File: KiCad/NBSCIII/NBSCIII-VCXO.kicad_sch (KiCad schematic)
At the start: 20 parts, among them Q1000 BC337-25, Q1001 2SC1906, X1000 6.000Mhz HC49/U

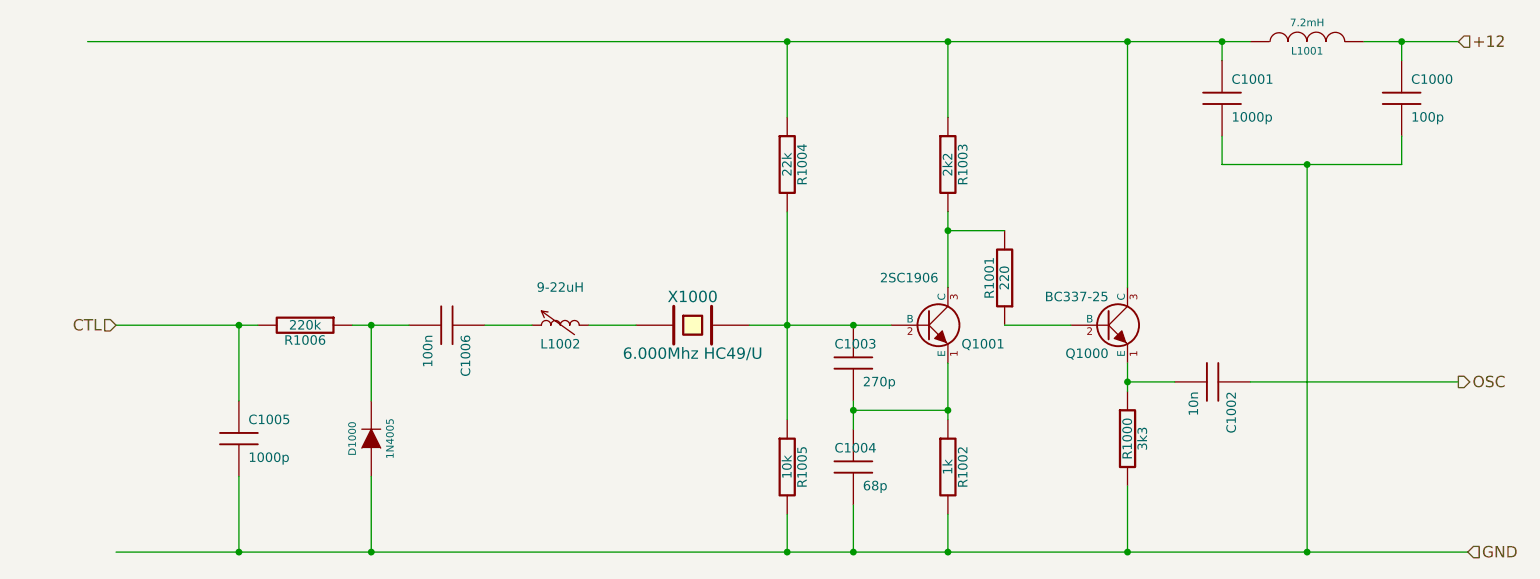
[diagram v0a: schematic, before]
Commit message: unrescue to Device:C
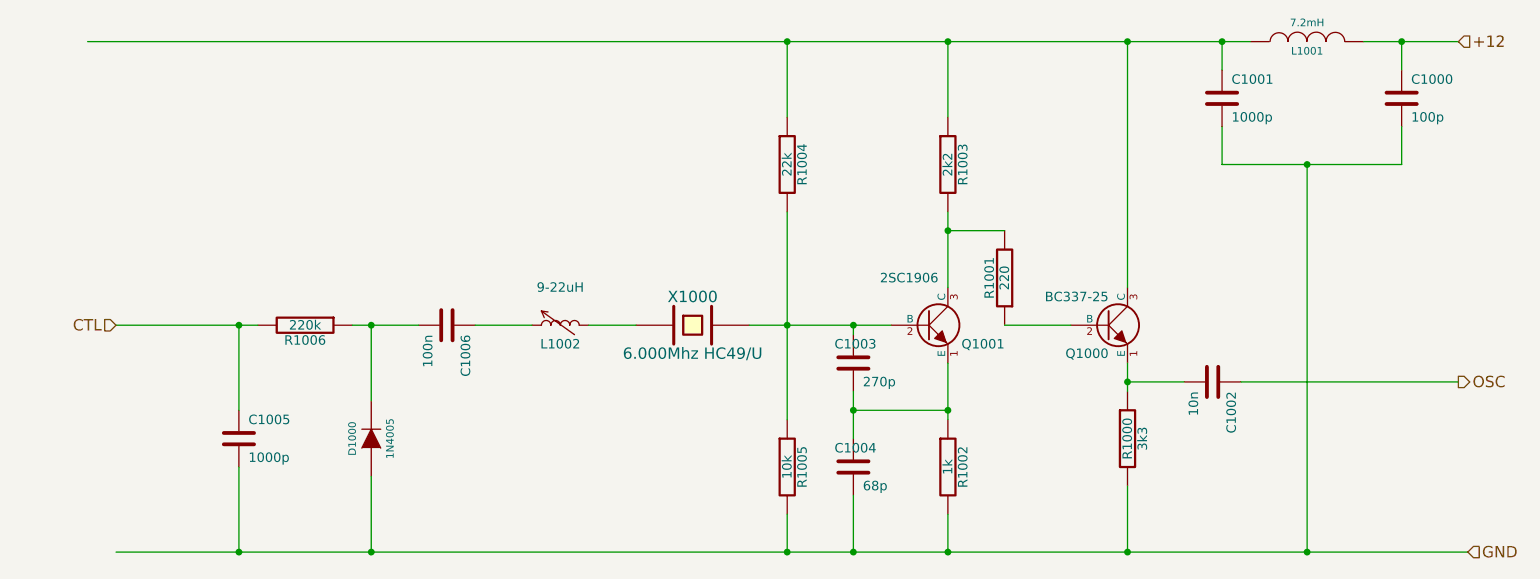
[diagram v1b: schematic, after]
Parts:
- C1000, C1001, C1002, C1003, C1004, C1005, C1006: symbol NBSCIII-rescue:C -> Device:C
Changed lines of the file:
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@@
   (junction (at 219.71 54.61) (diameter 0) (color 0 0 0 0)
   )
+  (junction (at 146.05 92.71) (diameter 0) (color 0 0 0 0)
+  )
   (junction (at 182.88 123.19) (diameter 0) (color 0 0 0 0)
   )
@@
   (junction (at 182.88 100.33) (diameter 0) (color 0 0 0 0)
   )
-  (junction (at 146.05 92.71) (diameter 0) (color 0 0 0 0)
-  )
   (junction (at 207.01 71.12) (diameter 0) (color 0 0 0 0)
   )
@@
   (junction (at 158.75 54.61) (diameter 0) (color 0 0 0 0)
   )
-  (wire (pts (xy 189.23 100.33) (xy 182.88 100.33))
-    (stroke (width 0) (type default) (color 0 0 0 0))
-  )
-  (wire (pts (xy 151.13 92.71) (xy 146.05 92.71))
-    (stroke (width 0) (type default) (color 0 0 0 0))
-  )
-  (wire (pts (xy 195.58 54.61) (xy 195.58 57.15))
+  (wire (pts (xy 146.05 104.14) (xy 146.05 107.95))
+    (stroke (width 0) (type default) (color 0 0 0 0))
+  )
+  (wire (pts (xy 182.88 100.33) (xy 190.5 100.33))
+    (stroke (width 0) (type default) (color 0 0 0 0))
+  )
+  (wire (pts (xy 195.58 54.61) (xy 195.58 58.42))
     (stroke (width 0) (type default) (color 0 0 0 0))
   )
@@
     (stroke (width 0) (type default) (color 0 0 0 0))
   )
-  (wire (pts (xy 86.36 92.71) (xy 81.28 92.71))
+  (wire (pts (xy 81.28 92.71) (xy 87.63 92.71))
     (stroke (width 0) (type default) (color 0 0 0 0))
   )
@@
     (stroke (width 0) (type default) (color 0 0 0 0))
   )
-  (wire (pts (xy 195.58 71.12) (xy 195.58 67.31))
+  (wire (pts (xy 146.05 92.71) (xy 151.13 92.71))
     (stroke (width 0) (type default) (color 0 0 0 0))
   )
@@
     (stroke (width 0) (type default) (color 0 0 0 0))
   )
-  (wire (pts (xy 146.05 106.68) (xy 146.05 104.14))
-    (stroke (width 0) (type default) (color 0 0 0 0))
-  )
   (wire (pts (xy 195.58 54.61) (xy 182.88 54.61))
     (stroke (width 0) (type default) (color 0 0 0 0))
@@
     (stroke (width 0) (type default) (color 0 0 0 0))
   )
+  (wire (pts (xy 219.71 54.61) (xy 219.71 58.42))
+    (stroke (width 0) (type default) (color 0 0 0 0))
+  )
   (wire (pts (xy 182.88 101.6) (xy 182.88 100.33))
     (stroke (width 0) (type default) (color 0 0 0 0))
   )
-  (wire (pts (xy 146.05 104.14) (xy 146.05 102.87))
+  (wire (pts (xy 146.05 101.6) (xy 146.05 104.14))
     (stroke (width 0) (type default) (color 0 0 0 0))
   )
@@
     (stroke (width 0) (type default) (color 0 0 0 0))
   )
-  (wire (pts (xy 219.71 54.61) (xy 219.71 57.15))
-    (stroke (width 0) (type default) (color 0 0 0 0))
-  )
   (wire (pts (xy 207.01 123.19) (xy 228.6 123.19))
     (stroke (width 0) (type default) (color 0 0 0 0))
   )
-  (wire (pts (xy 96.52 92.71) (xy 102.87 92.71))
+  (wire (pts (xy 95.25 92.71) (xy 102.87 92.71))
     (stroke (width 0) (type default) (color 0 0 0 0))
   )
@@
     (stroke (width 0) (type default) (color 0 0 0 0))
   )
-  (wire (pts (xy 219.71 67.31) (xy 219.71 71.12))
+  (wire (pts (xy 219.71 66.04) (xy 219.71 71.12))
     (stroke (width 0) (type default) (color 0 0 0 0))
   )
@@
     (stroke (width 0) (type default) (color 0 0 0 0))
   )
-  (wire (pts (xy 146.05 92.71) (xy 137.16 92.71))
-    (stroke (width 0) (type default) (color 0 0 0 0))
-  )
-  (wire (pts (xy 146.05 123.19) (xy 146.05 116.84))
+  (wire (pts (xy 137.16 92.71) (xy 146.05 92.71))
+    (stroke (width 0) (type default) (color 0 0 0 0))
+  )
+  (wire (pts (xy 195.58 66.04) (xy 195.58 71.12))
+    (stroke (width 0) (type default) (color 0 0 0 0))
+  )
+  (wire (pts (xy 146.05 115.57) (xy 146.05 123.19))
     (stroke (width 0) (type default) (color 0 0 0 0))
   )
@@
     (stroke (width 0) (type default) (color 0 0 0 0))
   )
-  (wire (pts (xy 63.5 113.03) (xy 63.5 123.19))
-    (stroke (width 0) (type default) (color 0 0 0 0))
-  )
   (wire (pts (xy 137.16 54.61) (xy 43.18 54.61))
     (stroke (width 0) (type default) (color 0 0 0 0))
@@
     (stroke (width 0) (type default) (color 0 0 0 0))
   )
-  (wire (pts (xy 63.5 92.71) (xy 63.5 102.87))
+  (wire (pts (xy 63.5 92.71) (xy 63.5 104.14))
     (stroke (width 0) (type default) (color 0 0 0 0))
   )
@@
     (stroke (width 0) (type default) (color 0 0 0 0))
   )
+  (wire (pts (xy 63.5 111.76) (xy 63.5 123.19))
+    (stroke (width 0) (type default) (color 0 0 0 0))
+  )
+  (wire (pts (xy 146.05 92.71) (xy 146.05 93.98))
+    (stroke (width 0) (type default) (color 0 0 0 0))
+  )
   (wire (pts (xy 219.71 71.12) (xy 207.01 71.12))
     (stroke (width 0) (type default) (color 0 0 0 0))
   )
-  (wire (pts (xy 199.39 100.33) (xy 227.33 100.33))
+  (wire (pts (xy 198.12 100.33) (xy 227.33 100.33))
     (stroke (width 0) (type default) (color 0 0 0 0))
   )
@@
     (pin "2")
   )
-  (symbol (lib_id "NBSCIII-rescue:C") (at 195.58 62.23 0) (unit 1)
+  (symbol (lib_id "Device:C") (at 195.58 62.23 0) (unit 1)
     (in_bom yes) (on_board yes)
     (property "Reference" "C1001" (id 0) (at 196.85 59.69 0)
@@
     (pin "2")
   )
-  (symbol (lib_id "NBSCIII-rescue:C") (at 219.71 62.23 0) (unit 1)
+  (symbol (lib_id "Device:C") (at 219.71 62.23 0) (unit 1)
     (in_bom yes) (on_board yes)
     (property "Reference" "C1000" (id 0) (at 220.98 59.69 0)
@@
     (pin "2")
   )
-  (symbol (lib_id "NBSCIII-rescue:C") (at 194.31 100.33 270) (unit 1)
+  (symbol (lib_id "Device:C") (at 194.31 100.33 270) (unit 1)
     (in_bom yes) (on_board yes)
     (property "Reference" "C1002" (id 0) (at 196.85 101.6 0)
@@
     (pin "2")
   )
-  (symbol (lib_id "NBSCIII-rescue:C") (at 146.05 111.76 0) (unit 1)
+  (symbol (lib_id "Device:C") (at 146.05 111.76 0) (unit 1)
     (in_bom yes) (on_board yes)
     (property "Reference" "C1004" (id 0) (at 143.51 109.22 0)
@@
     (pin "2")
   )
-  (symbol (lib_id "NBSCIII-rescue:C") (at 146.05 97.79 0) (unit 1)
+  (symbol (lib_id "Device:C") (at 146.05 97.79 0) (unit 1)
     (in_bom yes) (on_board yes)
     (property "Reference" "C1003" (id 0) (at 143.51 95.25 0)
@@
     (pin "2")
   )
-  (symbol (lib_id "NBSCIII-rescue:C") (at 91.44 92.71 270) (unit 1)
+  (symbol (lib_id "Device:C") (at 91.44 92.71 270) (unit 1)
     (in_bom yes) (on_board yes)
     (property "Reference" "C1006" (id 0) (at 93.98 93.98 0)
@@
     (pin "2")
   )
-  (symbol (lib_id "NBSCIII-rescue:C") (at 63.5 107.95 0) (unit 1)
+  (symbol (lib_id "Device:C") (at 63.5 107.95 0) (unit 1)
     (in_bom yes) (on_board yes)
     (property "Reference" "C1005" (id 0) (at 64.77 105.41 0)

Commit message: unrescue Device:R
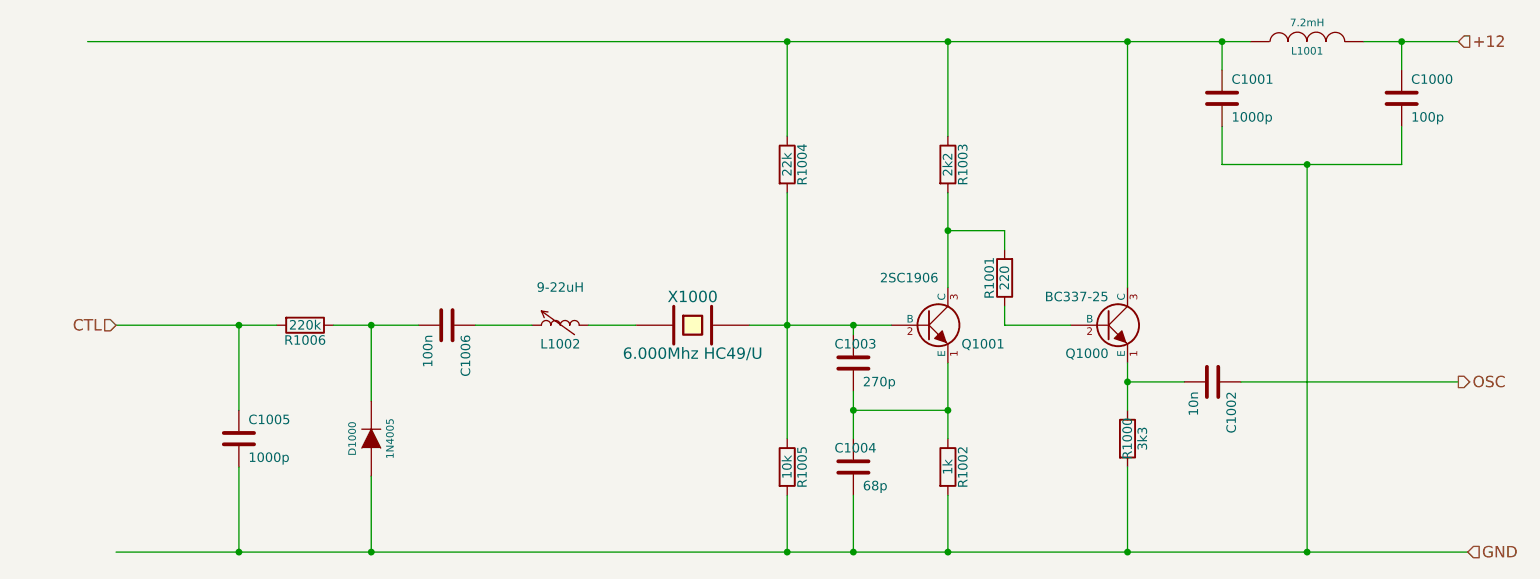
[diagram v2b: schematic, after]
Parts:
- 3k3, R1001, R1002, R1003, R1004, R1005, R1006: symbol NBSCIII-rescue:R -> Device:R
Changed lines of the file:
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@@
+    (stroke (width 0) (type default) (color 0 0 0 0))
+  )
+  (wire (pts (xy 63.5 92.71) (xy 68.58 92.71))
     (stroke (width 0) (type default) (color 0 0 0 0))
   )
@@
     (stroke (width 0) (type default) (color 0 0 0 0))
   )
-  (wire (pts (xy 137.16 123.19) (xy 137.16 118.11))
+  (wire (pts (xy 137.16 115.57) (xy 137.16 123.19))
     (stroke (width 0) (type default) (color 0 0 0 0))
   )
@@
     (stroke (width 0) (type default) (color 0 0 0 0))
   )
-  (wire (pts (xy 182.88 123.19) (xy 182.88 114.3))
+  (wire (pts (xy 182.88 111.76) (xy 182.88 123.19))
     (stroke (width 0) (type default) (color 0 0 0 0))
   )
@@
     (stroke (width 0) (type default) (color 0 0 0 0))
   )
-  (wire (pts (xy 137.16 92.71) (xy 137.16 77.47))
-    (stroke (width 0) (type default) (color 0 0 0 0))
-  )
-  (wire (pts (xy 66.04 92.71) (xy 63.5 92.71))
-    (stroke (width 0) (type default) (color 0 0 0 0))
-  )
   (wire (pts (xy 158.75 80.01) (xy 166.37 80.01))
     (stroke (width 0) (type default) (color 0 0 0 0))
   )
-  (wire (pts (xy 158.75 54.61) (xy 158.75 64.77))
+  (wire (pts (xy 158.75 54.61) (xy 158.75 67.31))
     (stroke (width 0) (type default) (color 0 0 0 0))
   )
@@
     (stroke (width 0) (type default) (color 0 0 0 0))
   )
-  (wire (pts (xy 158.75 123.19) (xy 158.75 118.11))
+  (wire (pts (xy 158.75 115.57) (xy 158.75 123.19))
+    (stroke (width 0) (type default) (color 0 0 0 0))
+  )
+  (wire (pts (xy 166.37 90.17) (xy 166.37 92.71))
     (stroke (width 0) (type default) (color 0 0 0 0))
   )
@@
     (stroke (width 0) (type default) (color 0 0 0 0))
   )
+  (wire (pts (xy 158.75 74.93) (xy 158.75 80.01))
+    (stroke (width 0) (type default) (color 0 0 0 0))
+  )
   (wire (pts (xy 182.88 87.63) (xy 182.88 54.61))
     (stroke (width 0) (type default) (color 0 0 0 0))
   )
+  (wire (pts (xy 166.37 80.01) (xy 166.37 82.55))
+    (stroke (width 0) (type default) (color 0 0 0 0))
+  )
   (wire (pts (xy 158.75 97.79) (xy 158.75 104.14))
     (stroke (width 0) (type default) (color 0 0 0 0))
   )
-  (wire (pts (xy 137.16 105.41) (xy 137.16 92.71))
-    (stroke (width 0) (type default) (color 0 0 0 0))
-  )
-  (wire (pts (xy 158.75 80.01) (xy 158.75 77.47))
-    (stroke (width 0) (type default) (color 0 0 0 0))
-  )
   (wire (pts (xy 195.58 54.61) (xy 182.88 54.61))
     (stroke (width 0) (type default) (color 0 0 0 0))
@@
     (stroke (width 0) (type default) (color 0 0 0 0))
   )
-  (wire (pts (xy 182.88 101.6) (xy 182.88 100.33))
+  (wire (pts (xy 182.88 100.33) (xy 182.88 104.14))
     (stroke (width 0) (type default) (color 0 0 0 0))
   )
@@
     (stroke (width 0) (type default) (color 0 0 0 0))
   )
-  (wire (pts (xy 137.16 64.77) (xy 137.16 54.61))
+  (wire (pts (xy 137.16 54.61) (xy 137.16 67.31))
     (stroke (width 0) (type default) (color 0 0 0 0))
   )
@@
     (stroke (width 0) (type default) (color 0 0 0 0))
   )
-  (wire (pts (xy 81.28 92.71) (xy 78.74 92.71))
+  (wire (pts (xy 76.2 92.71) (xy 81.28 92.71))
     (stroke (width 0) (type default) (color 0 0 0 0))
   )
@@
     (stroke (width 0) (type default) (color 0 0 0 0))
   )
+  (wire (pts (xy 137.16 92.71) (xy 137.16 107.95))
+    (stroke (width 0) (type default) (color 0 0 0 0))
+  )
   (wire (pts (xy 81.28 123.19) (xy 81.28 113.03))
     (stroke (width 0) (type default) (color 0 0 0 0))
@@
     (stroke (width 0) (type default) (color 0 0 0 0))
   )
-  (wire (pts (xy 158.75 104.14) (xy 158.75 105.41))
+  (wire (pts (xy 158.75 104.14) (xy 158.75 107.95))
+    (stroke (width 0) (type default) (color 0 0 0 0))
+  )
+  (wire (pts (xy 137.16 74.93) (xy 137.16 92.71))
     (stroke (width 0) (type default) (color 0 0 0 0))
   )
@@
     (pin "3")
   )
-  (symbol (lib_id "NBSCIII-rescue:R") (at 182.88 107.95 0) (unit 1)
+  (symbol (lib_id "Device:R") (at 182.88 107.95 0) (unit 1)
     (in_bom yes) (on_board yes)
     (property "Reference" "3k3" (id 0) (at 184.912 107.95 90))
@@
     (pin "2")
   )
-  (symbol (lib_id "NBSCIII-rescue:R") (at 166.37 86.36 180) (unit 1)
+  (symbol (lib_id "Device:R") (at 166.37 86.36 180) (unit 1)
     (in_bom yes) (on_board yes)
     (property "Reference" "R1001" (id 0) (at 164.338 86.36 90))
@@
     (pin "3")
   )
-  (symbol (lib_id "NBSCIII-rescue:R") (at 158.75 111.76 0) (unit 1)
+  (symbol (lib_id "Device:R") (at 158.75 111.76 0) (unit 1)
     (in_bom yes) (on_board yes)
     (property "Reference" "R1002" (id 0) (at 160.782 111.76 90))
@@
     (pin "2")
   )
-  (symbol (lib_id "NBSCIII-rescue:R") (at 158.75 71.12 0) (unit 1)
+  (symbol (lib_id "Device:R") (at 158.75 71.12 0) (unit 1)
     (in_bom yes) (on_board yes)
     (property "Reference" "R1003" (id 0) (at 160.782 71.12 90))
@@
     (pin "2")
   )
-  (symbol (lib_id "NBSCIII-rescue:R") (at 137.16 71.12 0) (unit 1)
+  (symbol (lib_id "Device:R") (at 137.16 71.12 0) (unit 1)
     (in_bom yes) (on_board yes)
     (property "Reference" "R1004" (id 0) (at 139.192 71.12 90))
@@
     (pin "2")
   )
-  (symbol (lib_id "NBSCIII-rescue:R") (at 137.16 111.76 0) (unit 1)
+  (symbol (lib_id "Device:R") (at 137.16 111.76 0) (unit 1)
     (in_bom yes) (on_board yes)
     (property "Reference" "R1005" (id 0) (at 139.192 111.76 90))
@@
     (pin "2")
   )
-  (symbol (lib_id "NBSCIII-rescue:R") (at 72.39 92.71 270) (unit 1)
+  (symbol (lib_id "Device:R") (at 72.39 92.71 270) (unit 1)
     (in_bom yes) (on_board yes)
     (property "Reference" "R1006" (id 0) (at 72.39 94.742 90))

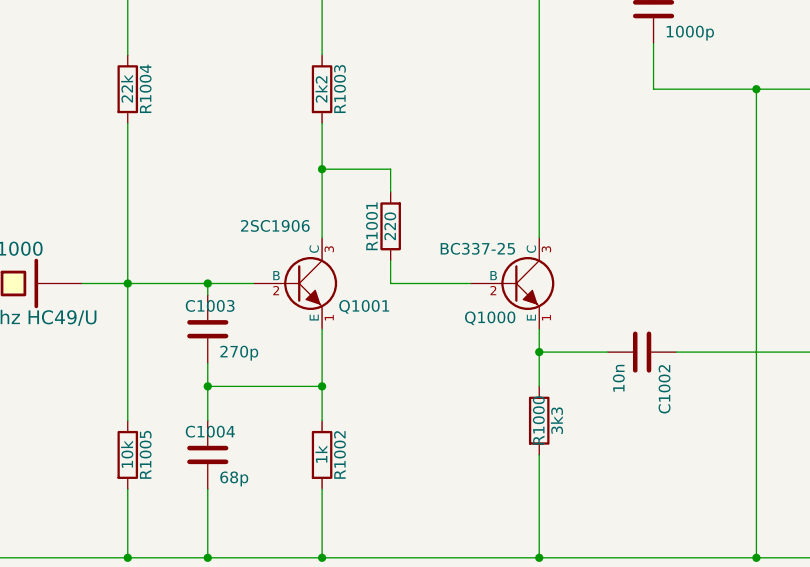
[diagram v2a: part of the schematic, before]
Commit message: unrescue NPN
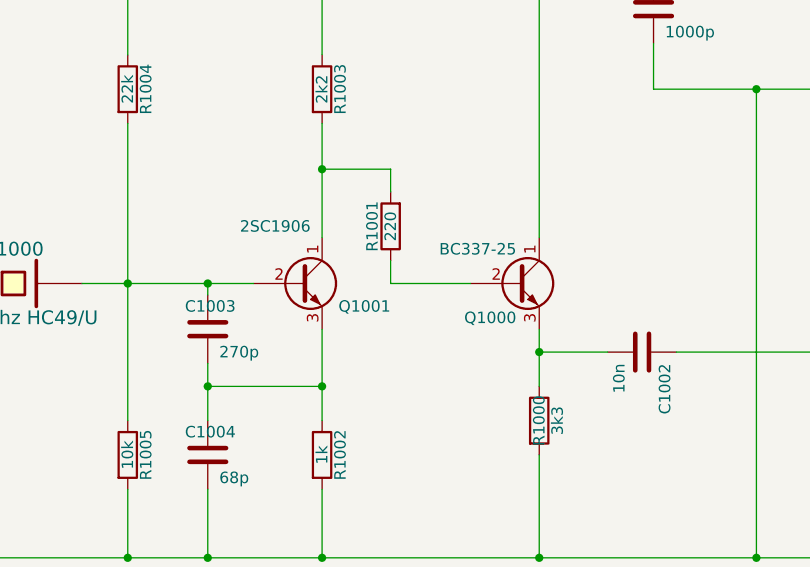
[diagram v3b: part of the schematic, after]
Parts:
- Q1000, Q1001: symbol NBSCIII-rescue:NPN -> Device:Q_NPN_CBE
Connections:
- net at C1001.1, L1001.1, R1003.1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: now also Q1000.1 (C); no longer Q1000.3 (C)
- net at 3k3.1, C1002.2: now also Q1000.3 (E); no longer Q1000.1 (E)
- net at R1001.2, R1003.2: now also Q1001.1 (C); no longer Q1001.3 (C)
- net at C1003.2, C1004.1, R1002.1: now also Q1001.3 (E); no longer Q1001.1 (E)
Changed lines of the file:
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@@
     (pin "2")
   )
-  (symbol (lib_id "NBSCIII-rescue:NPN") (at 180.34 92.71 0) (unit 1)
+  (symbol (lib_id "Device:Q_NPN_CBE") (at 180.34 92.71 0) (unit 1)
     (in_bom yes) (on_board yes)
     (property "Reference" "Q1000" (id 0) (at 180.34 96.52 0)
@@
     (pin "2")
   )
-  (symbol (lib_id "NBSCIII-rescue:NPN") (at 156.21 92.71 0) (unit 1)
+  (symbol (lib_id "Device:Q_NPN_CBE") (at 156.21 92.71 0) (unit 1)
     (in_bom yes) (on_board yes)
     (property "Reference" "Q1001" (id 0) (at 166.37 95.25 0)

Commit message: unrescue Device:D
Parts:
- D1000: symbol NBSCIII-rescue:DIODE -> Device:D
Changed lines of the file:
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@@
     (stroke (width 0) (type default) (color 0 0 0 0))
   )
-  (wire (pts (xy 81.28 92.71) (xy 81.28 102.87))
+  (wire (pts (xy 81.28 92.71) (xy 81.28 104.14))
     (stroke (width 0) (type default) (color 0 0 0 0))
   )
@@
     (stroke (width 0) (type default) (color 0 0 0 0))
   )
-  (wire (pts (xy 81.28 123.19) (xy 81.28 113.03))
+  (wire (pts (xy 81.28 111.76) (xy 81.28 123.19))
     (stroke (width 0) (type default) (color 0 0 0 0))
   )
@@
     (pin "2")
   )
-  (symbol (lib_id "NBSCIII-rescue:DIODE") (at 81.28 107.95 90) (unit 1)
+  (symbol (lib_id "Device:D") (at 81.28 107.95 90) (unit 1)
     (in_bom yes) (on_board yes)
     (property "Reference" "D1000" (id 0) (at 78.74 107.95 0)

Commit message: unrescue Device:L_small
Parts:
- L1001: symbol NBSCIII-rescue:INDUCTOR -> Device:L_Small
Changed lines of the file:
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@@
     (stroke (width 0) (type default) (color 0 0 0 0))
   )
-  (wire (pts (xy 199.39 54.61) (xy 195.58 54.61))
+  (wire (pts (xy 195.58 54.61) (xy 204.47 54.61))
     (stroke (width 0) (type default) (color 0 0 0 0))
   )
-  (wire (pts (xy 214.63 54.61) (xy 219.71 54.61))
+  (wire (pts (xy 209.55 54.61) (xy 219.71 54.61))
     (stroke (width 0) (type default) (color 0 0 0 0))
   )
@@
     (effects (font (size 1.524 1.524)) (justify left))
   )
-  (symbol (lib_id "NBSCIII-rescue:INDUCTOR") (at 207.01 54.61 90) (unit 1)
+  (symbol (lib_id "Device:L_Small") (at 207.01 54.61 90) (unit 1)
     (in_bom yes) (on_board yes)
     (property "Reference" "L1001" (id 0) (at 207.01 55.88 90)
